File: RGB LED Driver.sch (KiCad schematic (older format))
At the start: 32 parts, among them J1 UART, J2 LED_STRIP_OUTPUT, J3 5V_POWER_INPUT, J4 PWR_BTN, SW1 SW_Push, SW2 SW_Push, SW3 SW_Push, U1 ESP-12E, U2 AMS1117-3.3, U3 74LVC2G17

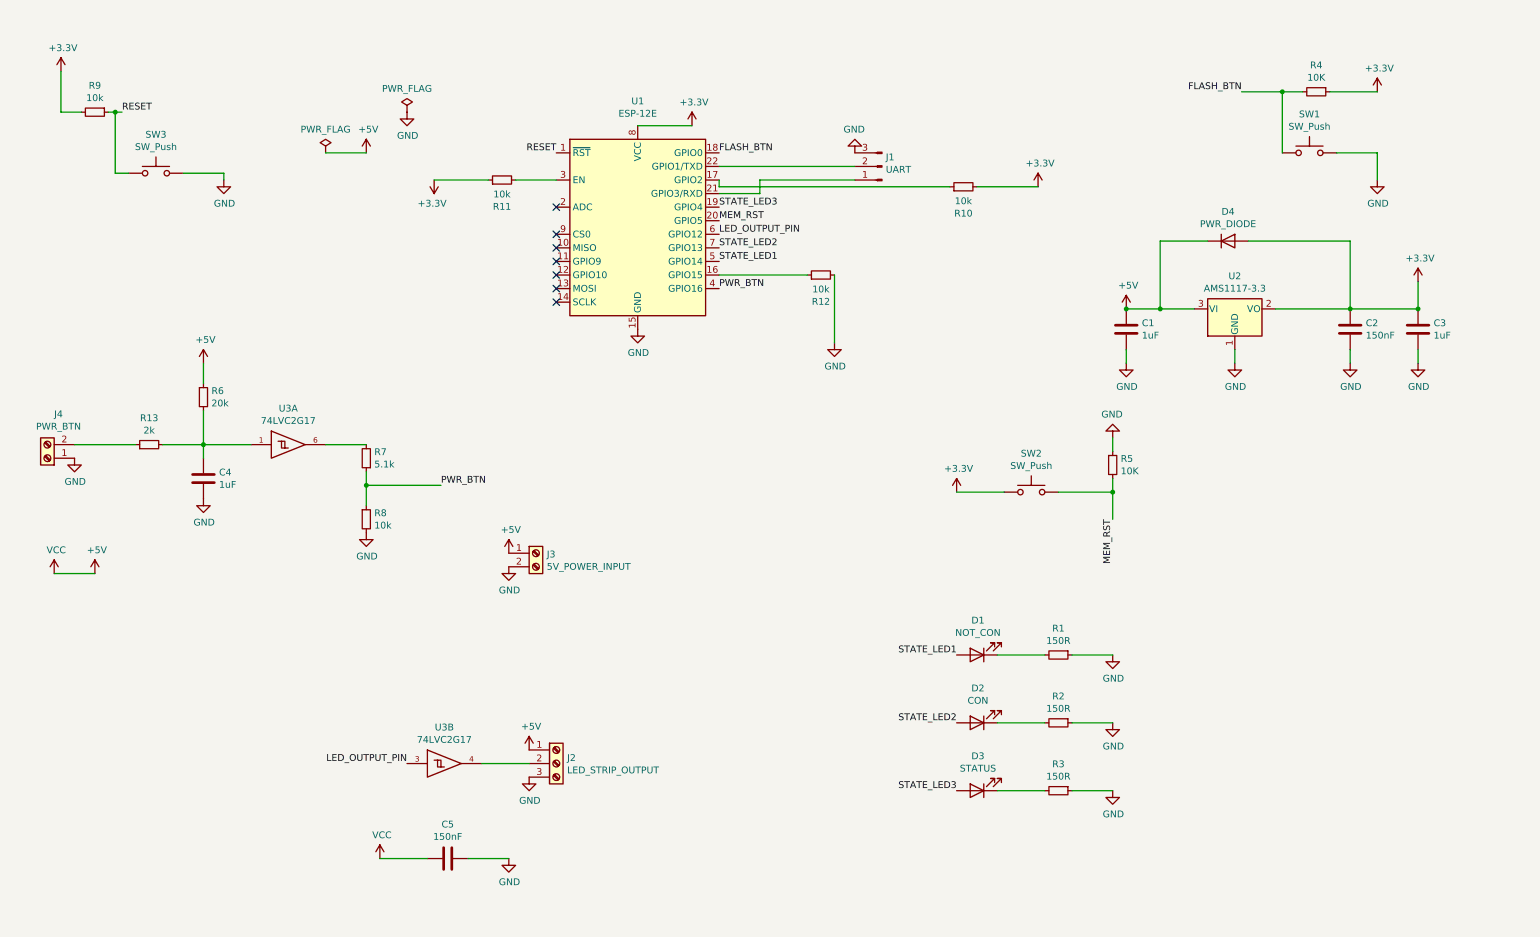
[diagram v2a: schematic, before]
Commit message: Schematic repaired and added 4 mounting holes + new 74lvc2g17
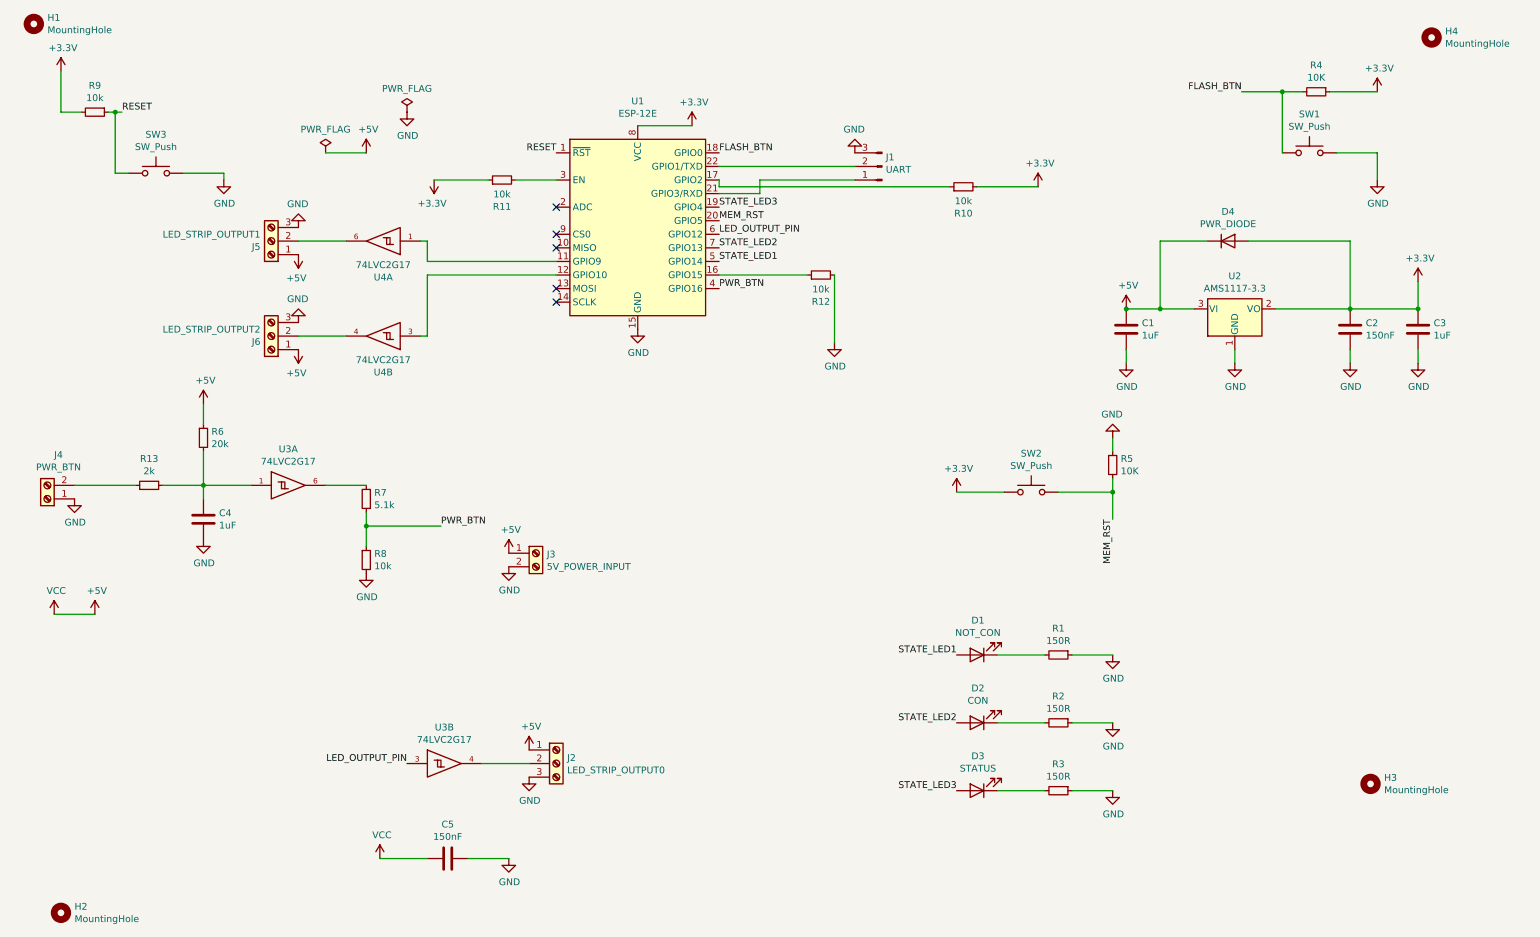
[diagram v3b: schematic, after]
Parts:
- added H1, H2, H3, H4: MountingHole, MountingHole:MountingHole_3.2mm_M3, symbol Mechanical:MountingHole
- added J5: LED_STRIP_OUTPUT1, TerminalBlock:TerminalBlock_Altech_AK300-3_P5.00mm, symbol Connector:Screw_Terminal_01x03
- added J6: LED_STRIP_OUTPUT2, TerminalBlock:TerminalBlock_Altech_AK300-3_P5.00mm, symbol Connector:Screw_Terminal_01x03
- added U4: 74LVC2G17, Package_TO_SOT_SMD:SOT-23-6_Handsoldering, symbol 74xGxx:74LVC2G17
- J2: value LED_STRIP_OUTPUT -> LED_STRIP_OUTPUT0
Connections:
- net +5V: now also J5.1 (Pin_1), J6.1 (Pin_1), U4.5 (VCC), U4.5 (VCC)
- net GND: now also J5.3 (Pin_3), J6.3 (Pin_3), U4.2 (GND), U4.2 (GND)
- net at U1.11 (GPIO9): now also U4.1
- net at U1.12 (GPIO10): now also U4.3
- new net: J6.2 (Pin_2), U4.4
- new net: J5.2 (Pin_2), U4.6
- no-connect marks 7 -> 5
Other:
- moved on the sheet: C4, J4, R13, R6, R7, R8, U3A

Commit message: PCB done, and ready for feedback
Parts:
- removed H1: MountingHole, MountingHole:MountingHole_3.2mm_M3, symbol Mechanical:MountingHole
- added C6: 150nF, Capacitor_SMD:C_0805_2012Metric_Pad1.18x1.45mm_HandSolder, symbol Device:C
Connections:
- net +5V: now also C6.2
- net GND: now also C6.1
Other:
- moved on the sheet: C5
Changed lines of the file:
@@
 L Device:C C5
 U 1 1 60B2DCC2
-P 3650 6750
-F 0 "C5" V 3398 6750 50  0000 C CNN
-F 1 "150nF" V 3489 6750 50  0000 C CNN
-F 2 "Capacitor_SMD:C_0805_2012Metric_Pad1.18x1.45mm_HandSolder" H 3688 6600 50  0001 C CNN
-F 3 "~" H 3650 6750 50  0001 C CNN
-	1    3650 6750
+P 2500 6750
+F 0 "C5" V 2248 6750 50  0000 C CNN
+F 1 "150nF" V 2339 6750 50  0000 C CNN
+F 2 "Capacitor_SMD:C_0805_2012Metric_Pad1.18x1.45mm_HandSolder" H 2538 6600 50  0001 C CNN
+F 3 "~" H 2500 6750 50  0001 C CNN
+	1    2500 6750
 	0    1    1    0
 $EndComp
@@
 L power:VCC #PWR0134
 U 1 1 606E692B
-P 3150 6750
-F 0 "#PWR0134" H 3150 6600 50  0001 C CNN
-F 1 "VCC" H 3165 6923 50  0000 C CNN
-F 2 "" H 3150 6750 50  0001 C CNN
-F 3 "" H 3150 6750 50  0001 C CNN
-	1    3150 6750
+P 2000 6750
+F 0 "#PWR0134" H 2000 6600 50  0001 C CNN
+F 1 "VCC" H 2015 6923 50  0000 C CNN
+F 2 "" H 2000 6750 50  0001 C CNN
+F 3 "" H 2000 6750 50  0001 C CNN
+	1    2000 6750
 	1    0    0    -1
 $EndComp
@@
 L power:GND #PWR0135
 U 1 1 606E70B4
-P 4100 6750
-F 0 "#PWR0135" H 4100 6500 50  0001 C CNN
-F 1 "GND" H 4105 6577 50  0000 C CNN
-F 2 "" H 4100 6750 50  0001 C CNN
-F 3 "" H 4100 6750 50  0001 C CNN
-	1    4100 6750
-	1    0    0    -1
-$EndComp
-Wire Wire Line
-	3800 6750 4100 6750
-Wire Wire Line
-	3500 6750 3150 6750
+P 2950 6750
+F 0 "#PWR0135" H 2950 6500 50  0001 C CNN
+F 1 "GND" H 2955 6577 50  0000 C CNN
+F 2 "" H 2950 6750 50  0001 C CNN
+F 3 "" H 2950 6750 50  0001 C CNN
+	1    2950 6750
+	1    0    0    -1
+$EndComp
+Wire Wire Line
+	2650 6750 2950 6750
+Wire Wire Line
+	2350 6750 2000 6750
 $Comp
 L Device:D D4
@@
 $EndComp
 $Comp
-L Mechanical:MountingHole H1
-U 1 1 607A223E
-P 600 600
-F 0 "H1" H 700 646 50  0000 L CNN
-F 1 "MountingHole" H 700 555 50  0000 L CNN
-F 2 "MountingHole:MountingHole_3.2mm_M3" H 600 600 50  0001 C CNN
-F 3 "~" H 600 600 50  0001 C CNN
-	1    600  600
-	1    0    0    -1
-$EndComp
-$Comp
 L Mechanical:MountingHole H2
 U 1 1 607A2961
@@
 	1    0    0    -1
 $EndComp
+$Comp
+L power:GND #PWR06
+U 1 1 60823248
+P 4400 6850
+F 0 "#PWR06" H 4400 6600 50  0001 C CNN
+F 1 "GND" H 4405 6677 50  0000 C CNN
+F 2 "" H 4400 6850 50  0001 C CNN
+F 3 "" H 4400 6850 50  0001 C CNN
+	1    4400 6850
+	1    0    0    -1
+$EndComp
+$Comp
+L Device:C C6
+U 1 1 60823B32
+P 4050 6850
+F 0 "C6" V 3798 6850 50  0000 C CNN
+F 1 "150nF" V 3889 6850 50  0000 C CNN
+F 2 "Capacitor_SMD:C_0805_2012Metric_Pad1.18x1.45mm_HandSolder" H 4088 6700 50  0001 C CNN
+F 3 "~" H 4050 6850 50  0001 C CNN
+	1    4050 6850
+	0    1    1    0
+$EndComp
+$Comp
+L power:VCC #PWR05
+U 1 1 60824279
+P 3650 6850
+F 0 "#PWR05" H 3650 6700 50  0001 C CNN
+F 1 "VCC" H 3665 7023 50  0000 C CNN
+F 2 "" H 3650 6850 50  0001 C CNN
+F 3 "" H 3650 6850 50  0001 C CNN
+	1    3650 6850
+	1    0    0    -1
+$EndComp
+Wire Wire Line
+	4200 6850 4400 6850
+Wire Wire Line
+	3650 6850 3900 6850
 $EndSCHEMATC

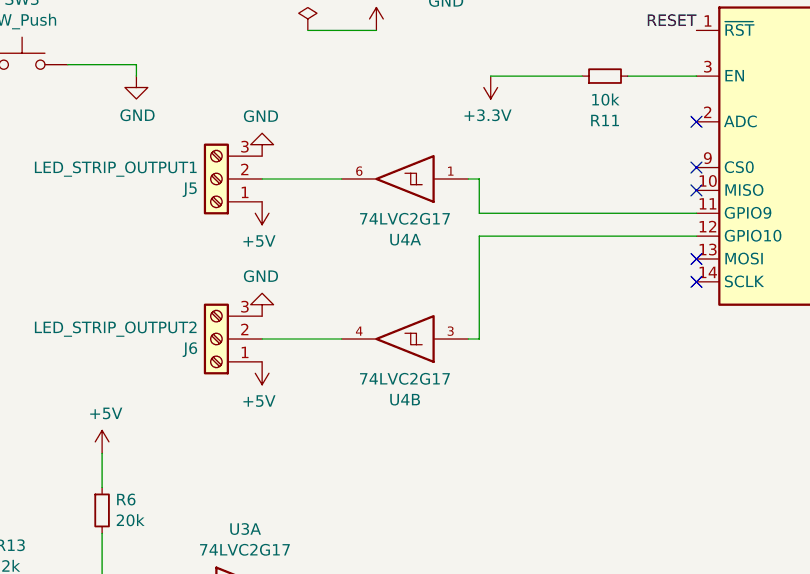
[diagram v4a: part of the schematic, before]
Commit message: PCB updated and fixed problems
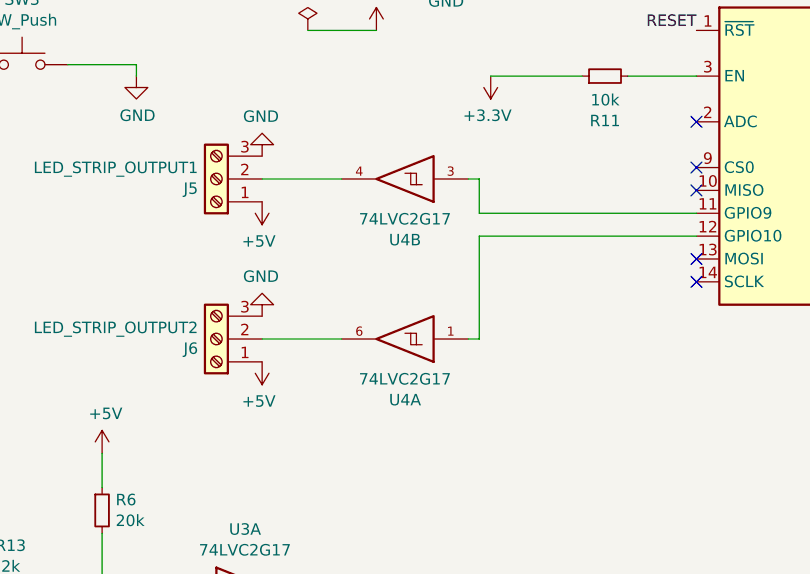
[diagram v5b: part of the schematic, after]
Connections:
- net at U1.11 (GPIO9): now also U4.3; no longer U4.1
- net at U1.12 (GPIO10): now also U4.1; no longer U4.3
- net at U4.4: now also J5.2 (Pin_2); no longer J6.2 (Pin_2)
- net at U4.6: now also J6.2 (Pin_2); no longer J5.2 (Pin_2)
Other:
- moved on the sheet: U4A, U4B
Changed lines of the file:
@@
 L 74xGxx:74LVC2G17 U4
 U 2 1 6071A724
+P 3150 2200
+F 0 "U4" H 3125 2467 50  0000 C CNN
+F 1 "74LVC2G17" H 3125 2376 50  0000 C CNN
+F 2 "Package_TO_SOT_SMD:SOT-23-6_Handsoldering" H 3150 2200 50  0001 C CNN
+F 3 "http://www.ti.com/lit/sg/scyt129e/scyt129e.pdf" H 3150 2200 50  0001 C CNN
+	2    3150 2200
+	-1   0    0    1
+$EndComp
+$Comp
+L 74xGxx:74LVC2G17 U4
+U 1 1 60720DDC
 P 3150 2900
 F 0 "U4" H 3125 3167 50  0000 C CNN
@@
 F 2 "Package_TO_SOT_SMD:SOT-23-6_Handsoldering" H 3150 2900 50  0001 C CNN
 F 3 "http://www.ti.com/lit/sg/scyt129e/scyt129e.pdf" H 3150 2900 50  0001 C CNN
-	2    3150 2900
-	-1   0    0    1
-$EndComp
-$Comp
-L 74xGxx:74LVC2G17 U4
-U 1 1 60720DDC
-P 3150 2200
-F 0 "U4" H 3125 2467 50  0000 C CNN
-F 1 "74LVC2G17" H 3125 2376 50  0000 C CNN
-F 2 "Package_TO_SOT_SMD:SOT-23-6_Handsoldering" H 3150 2200 50  0001 C CNN
-F 3 "http://www.ti.com/lit/sg/scyt129e/scyt129e.pdf" H 3150 2200 50  0001 C CNN
-	1    3150 2200
+	1    3150 2900
 	-1   0    0    1
 $EndComp
@@
 $EndComp
 Wire Wire Line
-	3500 2450 3500 2900
-Wire Wire Line
 	3500 2900 3450 2900
 $Comp
@@
 Wire Wire Line
 	3650 6850 3900 6850
+Wire Wire Line
+	3500 2450 3500 2900
 $EndSCHEMATC
